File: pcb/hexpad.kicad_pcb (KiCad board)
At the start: 2 copper layers, 76 x 74 mm, 12 parts, among them SW1 SW_MX, SW2 SW_MX, SW3 SW_MX, SW4 SW_MX, SW5 SW_MX, SW6 SW_MX, U1 XIAO-RP2040

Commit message: Fix PCB: move XIAO down 3mm to clear front switch holes
Resolves the hole-overlap (U1 pin1 vs SW2 center post) and mask-bridge DRC
errors. Remaining items are cosmetic (courtyard/silk) and don't affect Gerbers.
Board is placement-correct; signal routing to be redone at the new position.

Co-Authored-By: Claude Opus 4.8 <noreply@anthropic.com>
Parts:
- moved U1 3.00 mm to (-10.0, 27.0)

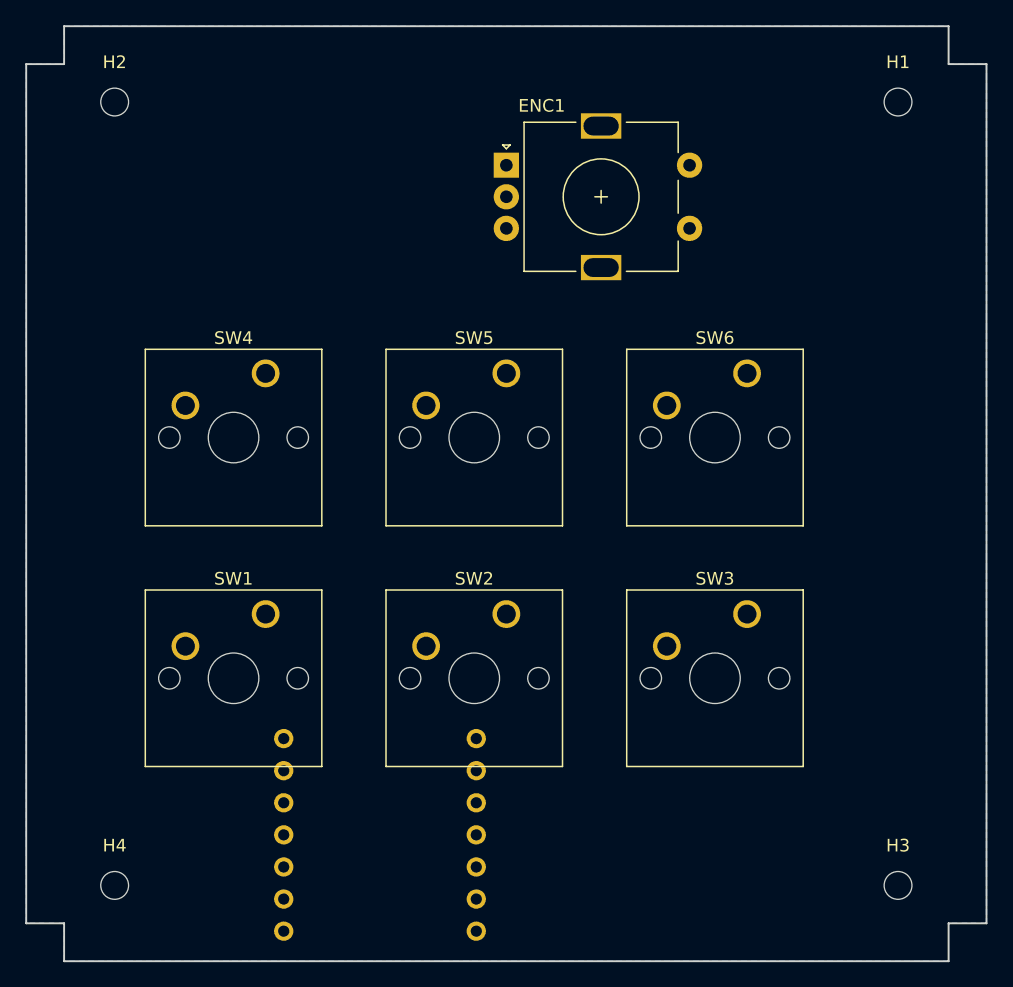
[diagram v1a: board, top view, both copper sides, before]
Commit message: Route hexpad PCB + export JLCPCB Gerbers
All 9 signal nets routed (interactive), DRC clean: 0 unconnected, 0 copper/
clearance/short/crossing violations. Remaining 4 DRC items are cosmetic
(courtyard/silk-over-copper) and do not affect fabrication.

Exported standard 2-layer Gerber set + Excellon drill (PTH/NPTH), zipped to
pcb/hexpad-gerbers.zip ready for JLCPCB upload.

Co-Authored-By: Claude Opus 4.8 <noreply@anthropic.com>
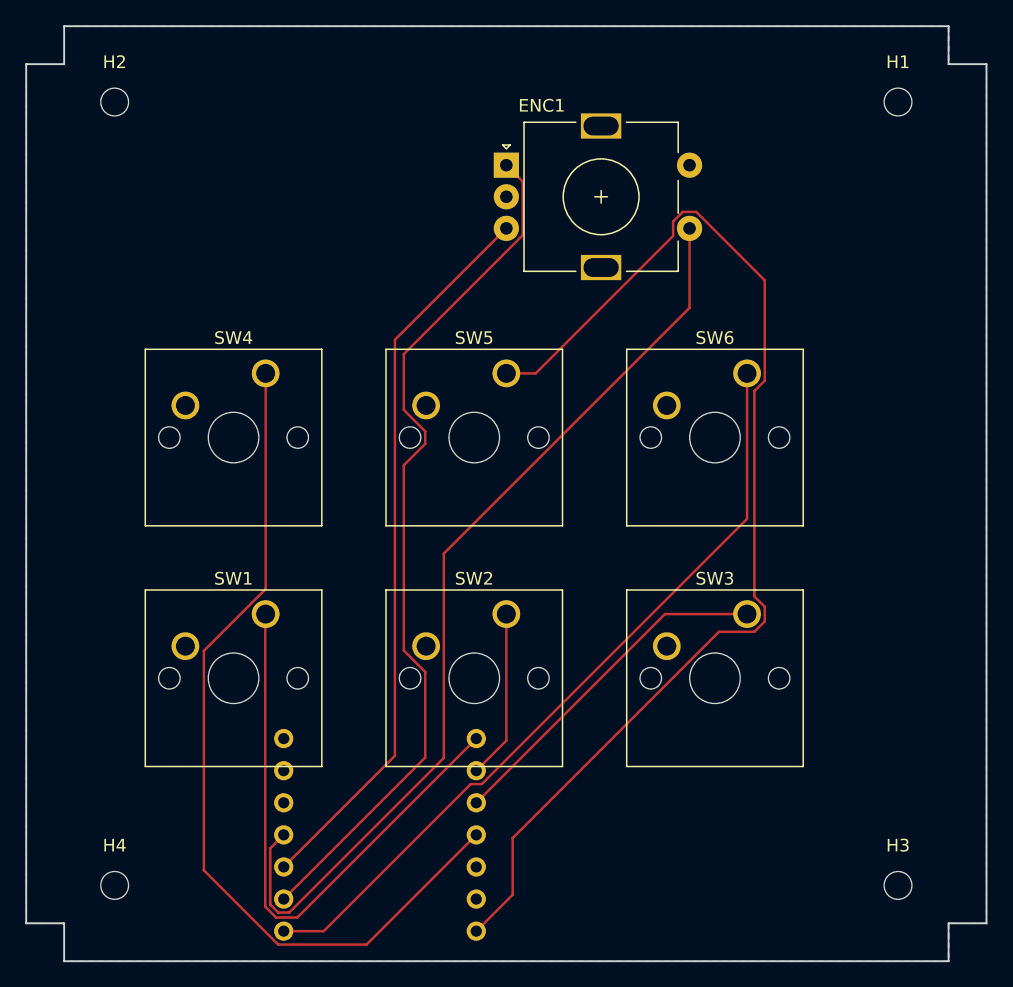
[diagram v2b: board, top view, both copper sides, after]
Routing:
- net SW5: track 0.00 -> 91.9 mm
- net ENCSW: track 0.00 -> 75.0 mm
- net ENCA: track 0.00 -> 69.3 mm
- net SW4: track 0.00 -> 68.9 mm
- net SW6: track 0.00 -> 61.7 mm
- net ENCB: track 0.00 -> 57.8 mm
- net SW1: track 0.00 -> 46.1 mm
- net SW3: track 0.00 -> 27.6 mm
- net SW2: track 0.00 -> 13.4 mm

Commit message: PCB: silk-brand "Hexpad", re-plot Gerbers, add render/pcb/schematic images
- build_hexpad_pcb.py adds "Hexpad" to F.SilkS; board + gerbers re-plotted so
  the silkscreen branding is included in hexpad-gerbers.zip.
- DRC: 0 errors, 0 unconnected (pth_inside_courtyard reclassified to warning --
  the XIAO is intentionally back-mounted under the front switches, a benign
  cross-layer courtyard overlap; remaining warnings are silk-over-copper).
- Schematic ERC verified clean (0 violations).
- docs/images/: render.png, pcb.png, schematic.png (case photo still TODO).

Co-Authored-By: Claude Opus 4.8 <noreply@anthropic.com>
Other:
- board text added: "Hexpad"
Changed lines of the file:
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@@
 		(layer "Edge.Cuts")
+	)
+	(gr_text "Hexpad"
+		(at 0 31 0)
+		(layer "F.SilkS")
+		(effects
+			(font
+				(size 2.2 2.2)
+				(thickness 0.3)
+			)
+		)
 	)
 	(segment

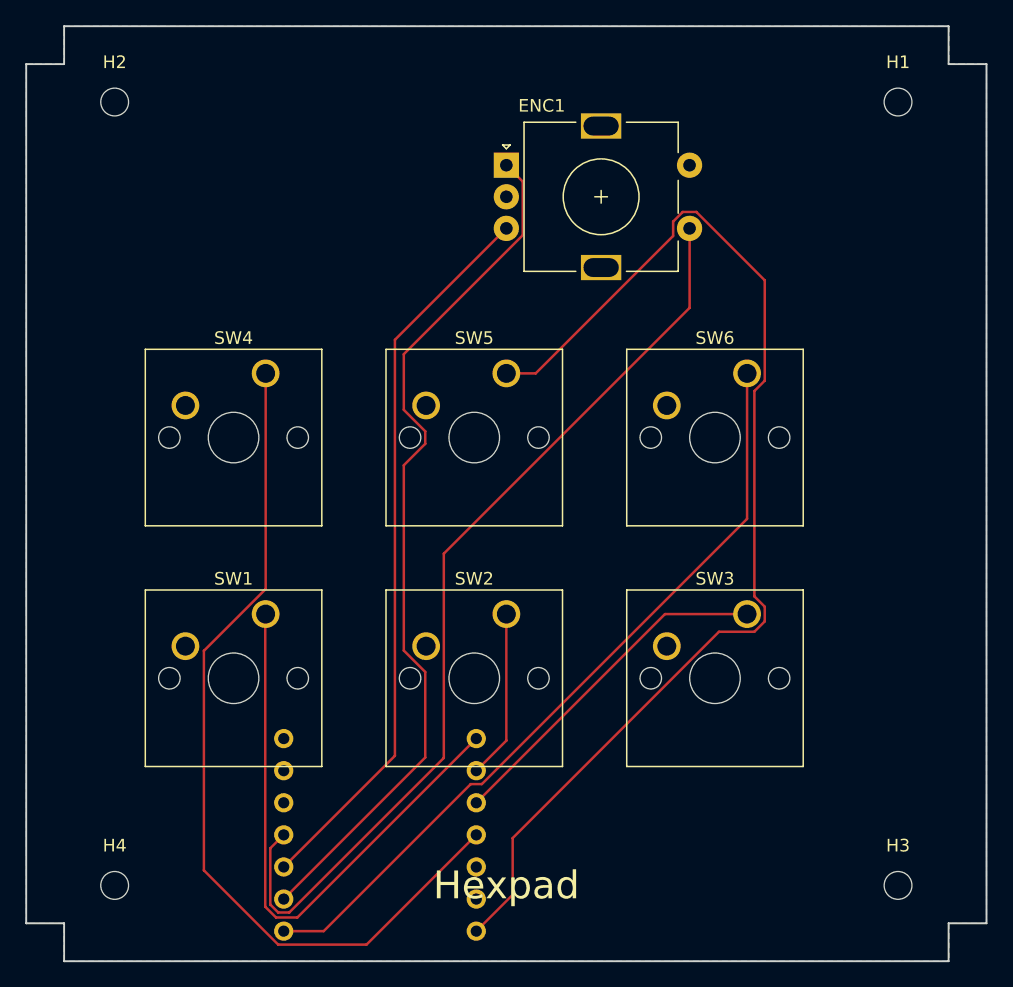
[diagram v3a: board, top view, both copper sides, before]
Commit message: fix: move mounting holes/posts to X=+/-32 to align with case (routing preserved)
The PCB holes and top-plate posts sat at X=+/-31, but the bottom-case screw
bosses are at X=+/-32, Y=+/-31 (verified from the STEP via circular-edge centers)
-- so the case didn't line up. Moved PCB holes + CAD posts to +/-32.

The board was regenerated by build_hexpad_pcb.py which wiped the interactive
routing; recovered the 58 routed segments from the prior commit and moved only
the 4 (net-less) mounting holes, so routing + GND pour + silk branding are intact.
DRC: 0 errors, 0 unconnected (courtyard severity re-set to warning). Gerbers
re-plotted to pcb/ and production/.

Co-Authored-By: Claude Opus 4.8 <noreply@anthropic.com>
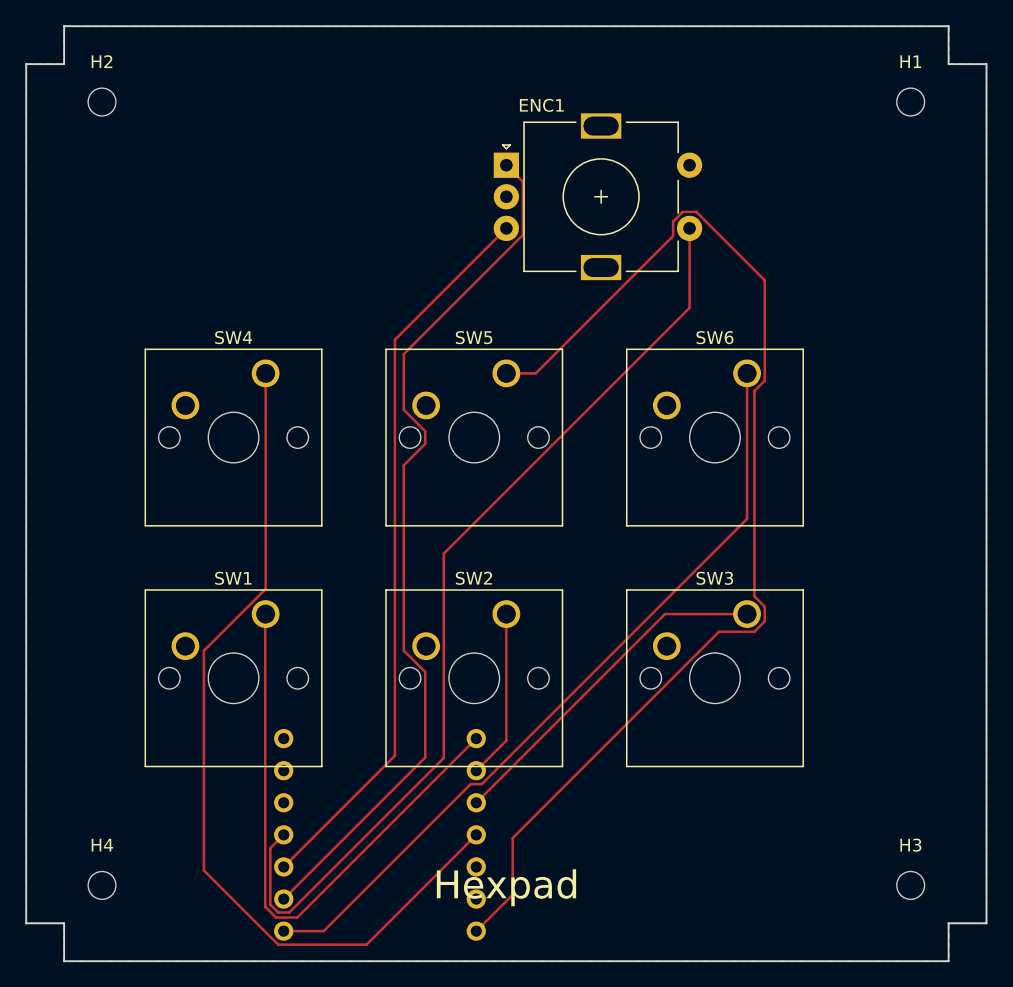
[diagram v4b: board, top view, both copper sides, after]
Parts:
- moved H1 1.00 mm to (32.0, -31.0)
- moved H2 1.00 mm to (-32.0, -31.0)
- moved H3 1.00 mm to (32.0, 31.0)
- moved H4 1.00 mm to (-32.0, 31.0)
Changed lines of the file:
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@@
 	(footprint "MountingHole_2.2mm_M2"
 		(layer "F.Cu")
-		(at 31 31)
+		(at 32 31)
 		(descr "Mounting Hole 2.2mm, M2, no annular, generated by kicad-footprint-generator mountinghole.py")
 		(tags "mountinghole M2")
@@
 	(footprint "MountingHole_2.2mm_M2"
 		(layer "F.Cu")
-		(at -31 31)
+		(at -32 31)
 		(descr "Mounting Hole 2.2mm, M2, no annular, generated by kicad-footprint-generator mountinghole.py")
 		(tags "mountinghole M2")
@@
 	(footprint "MountingHole_2.2mm_M2"
 		(layer "F.Cu")
-		(at 31 -31)
+		(at 32 -31)
 		(descr "Mounting Hole 2.2mm, M2, no annular, generated by kicad-footprint-generator mountinghole.py")
 		(tags "mountinghole M2")
@@
 	(footprint "MountingHole_2.2mm_M2"
 		(layer "F.Cu")
-		(at -31 -31)
+		(at -32 -31)
 		(descr "Mounting Hole 2.2mm, M2, no annular, generated by kicad-footprint-generator mountinghole.py")
 		(tags "mountinghole M2")
